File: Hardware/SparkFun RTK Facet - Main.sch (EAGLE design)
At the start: 99 parts, among them J1 QWIIC_RIGHT_ANGLE, J15 FPC_12_0.5MM2, J18 FPC_12_0.5MM2, J2 U.FL, J8 FPC_12_0.5MM2, Q2 MBT3904DW1T1, Q3 SIL2308, U1 74HC4052D, U10 MCP73833, U12 AP2112K-3.3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

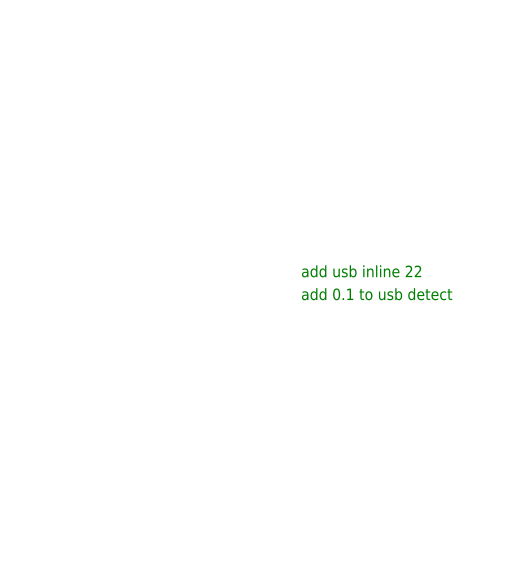
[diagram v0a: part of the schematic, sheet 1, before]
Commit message: Move display connector to side so overlay connector can be center. Notch PCBs. Add dummy PCB height. Add dummy retention plate.
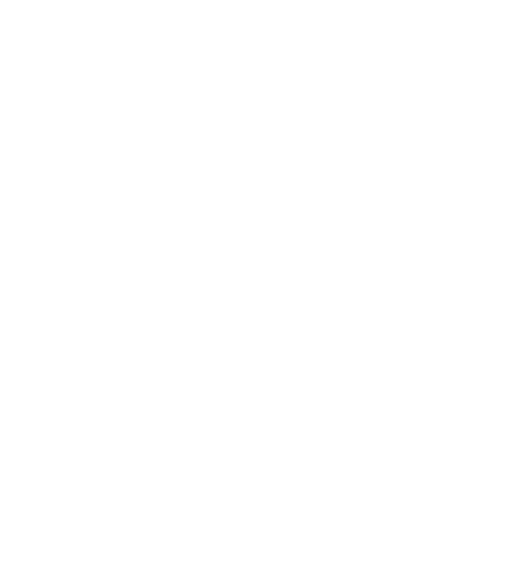
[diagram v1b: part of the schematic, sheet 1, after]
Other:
- note removed: "add 0.1 to usb detect"
- note removed: "add usb inline 22"
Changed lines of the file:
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@@
 <text x="332.74" y="132.08" size="1.27" layer="97" align="center">600mA Max
 55uA Quiescent</text>
-<text x="482.6" y="157.48" size="1.27" layer="91">add usb inline 22</text>
-<text x="482.6" y="154.94" size="1.27" layer="91">add 0.1 to usb detect</text>
 </plain>
 <instances>

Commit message: Update PROD ID on 12 pin connector. Add gerbers for v10.
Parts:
- J15, J18, J8: value FPC_12_0.5MM2 -> FPC_12_0.5MM_BACKFLIP; device RTK Facet:FPC_12_0.5MM2 -> RTK Facet:FPC_12_0.5MM_BACKFLIP
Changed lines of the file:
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@@
 <part name="SUPPLY7" library="SparkFun-PowerSymbols" deviceset="V_BATT" device=""/>
 <part name="GND20" library="SparkFun-PowerSymbols" deviceset="GND" device=""/>
-<part name="J15" library="RTK Facet" deviceset="FPC_12_0.5MM" device="2" value="FPC_12_0.5MM2"/>
+<part name="J15" library="RTK Facet" deviceset="FPC_12_0.5MM" device="_BACKFLIP" value="FPC_12_0.5MM_BACKFLIP"/>
 <part name="SUPPLY31" library="SparkFun-PowerSymbols" deviceset="3.3V" device=""/>
 <part name="GND28" library="SparkFun-PowerSymbols" deviceset="GND" device=""/>
-<part name="J18" library="RTK Facet" deviceset="FPC_12_0.5MM" device="2" value="FPC_12_0.5MM2"/>
+<part name="J18" library="RTK Facet" deviceset="FPC_12_0.5MM" device="_BACKFLIP" value="FPC_12_0.5MM_BACKFLIP"/>
 <part name="Q3" library="SparkFun-DiscreteSemi" deviceset="MOSFET_COMPLIMENTARY_PAIR" device="-SIL2308" value="SIL2308"/>
 <part name="C20" library="SparkFun-Capacitors" deviceset="22UF" device="-0603-6.3V-20%" value="22uF"/>
@@
 <part name="C29" library="SparkFun-Capacitors" deviceset="0.1UF" device="-0603-25V-5%" value="0.1uF"/>
 <part name="GND9" library="SparkFun-PowerSymbols" deviceset="GND" device=""/>
-<part name="J8" library="RTK Facet" deviceset="FPC_12_0.5MM" device="2" value="FPC_12_0.5MM2"/>
+<part name="J8" library="RTK Facet" deviceset="FPC_12_0.5MM" device="_BACKFLIP" value="FPC_12_0.5MM_BACKFLIP"/>
 </parts>
 <sheets>

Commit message: Move external connectors to button control. Add radio connector. Move ESP32 to VOUT. Move USB to VOUT. Remove USB from I2C.
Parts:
- removed J6: (no value), SparkFun-Connectors:CONN_041X04_NO_SILK_NO_POP
- added J10: FPC_12_0.5MM_BACKFLIP, RTK Facet:FPC_12_0.5MM_BACKFLIP
- added J3: (no value), SparkFun-Connectors:CONN_01PTH_NO_SILK_YES_STOP
- added J9: CORTEX_JTAG_DEBUG_PTH, SparkFun-Connectors:CORTEX_JTAG_DEBUG_PTH
- added JP1, JP2: JUMPER-SMT_2_NO_SILK, SparkFun-Jumpers:JUMPER-SMT_2_NO_SILK
- added R33, R34: 10k, SparkFun-Resistors:10KOHM-0603-1/10W-1%
- U4: value ADP160 -> STLQ015; device SparkFun-IC-Power:ADP160 -> SparkFun-IC-Power:STLQ015-3.3V
- U5: value ESP-WROOM-32NARROW -> ESP-WROOM-3232D-NARROW; device SparkFun-RF:ESP-WROOM-32NARROW -> SparkFun-RF:ESP-WROOM-3232D-NARROW
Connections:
- removed net ESP_0/BOOT: Q2Q2.C, U5.IO0
- removed net ESP_12/STAT_LED: R11.2, U5.MISO_H/IO12
- removed net ESP_13/POWER_CTRL: D4.A, R22.1, R24.2, U5.MOSI_H/IO13
- removed net ESP_14: J6.4, U5.SCK_H/IO14
- removed net ESP_15/FAST_OFF: C20.2, Q3G1.G, R24.1, U5.CS0_H/IO15
- removed net ESP_2/PERIPHERAL_POWER: R1.2, U12.EN, U5.IO2
- removed net ESP_27/ZED_!RESET!: R2D.2, U5.IO27
- removed net ESP_32: J6.3, U5.XTAL_P/IO32
- removed net ESP_33: J6.2, U5.XTAL_N/IO33
- removed net ESP_36/BATT_ALRT: U5.SENSOR_VP/I36, U7.!ALRT
- removed net ESP_4/MUX_A: U1.A, U5.IO4
- removed net ESP_5/MUX_B: U1.B, U5.CS0_V/IO5
- removed net ESP_I34/ZED_TX_READY: R9A.2, U5.I34
- removed net ESP_I35: J6.1, U5.I35
- new net ESP_0/BOOT/STAT_LED/MUX_B: Q2Q2.C, R11.2, U1.B, U5.IOA0
- new net ESP_12/MTDI/RADIO_NI: J10.4, J9.NC/TDI, U5.MISO2/IOA12
- new net ESP_13/POWER_CTRL/MTCK: D4.A, J9.SWDCLK/TCK, R22.1, R24.2, U5.MOSI2/IOA13
- new net ESP_14/PERIPHERAL_POWER/MTMS: J9.SWDIO/TMS, R1.2, U12.EN, U5.SCK2/IOA14
- new net ESP_15/MTDO/RADIO_!RESET!: J10.5, J9.SWO/TDO, U5.CS2/IOA15
- new net ESP_2/MUX_A: U1.A, U5.IOA2
- new net ESP_27/FAST_OFF: C20.2, Q3G1.G, R24.1, U5.IOA27
- new net ESP_32/RADIO_TXO: J10.11, U5.XTAL_P/IOA32
- new net ESP_33/RADIO_RXI: J10.10, U5.XTAL_N/IOA33
- new net ESP_4/RADIO_PWR_ON: J10.6, U5.IOA4
- new net ESP_5/RADIO_CTSI: J10.8, U5.CS3/IO5
- new net ESP_I34/RADIO_INT: J10.7, U5.IA34
- new net ESP_I35/DEVICE_SENSE: R33.2, R34.1, U5.IA35
- new net ESP_I36/RADIO_RTSO: J10.9, U5.SENSOR_VP/IA36
- new net N$21: JP1.2, U8.SDA
- new net N$23: JP2.2, U8.SCL/CFG0
- new net ZED_!RESET!: R2D.2
- new net ZED_TX_READY: R9A.2
- net 3.3V: now also J10.3; no longer C13.1, C14.1, R18.2, U6.V3, U6.VCC, U8.VDD33, U8.VDDA33
- net ESP32_EN: now also J9.!RESET
- net ESP32_RXI: now also U5.RX-IO3; no longer U5.RXD
- net ESP32_TXO: now also U5.TX-IO1; no longer U5.TXD
- net ESP_18/SD_SCK: now also U5.SCK3/IO18; no longer U5.SCK_V/IO18
- net ESP_19/SD_CIPO: now also U5.MISO3/IO19; no longer U5.MISO_V/IO19
- net ESP_21/SDA: now also JP1.1, U5.SDA/IO21; no longer U5.IO21, U8.SDA
- net ESP_22/SCL: now also JP2.1, U5.SCL/IO22; no longer U5.IO22, U8.SCL
- net ESP_23/SD_COPI: now also U5.MOSI3/IO23; no longer U5.MOSI_V/IO23
- net ESP_25/SD_!CS!: now also U5.DAC1/IOA25; no longer U5.IO25
- net ESP_26/DAC2: now also U5.DAC2/IOA26; no longer U5.IO26
- net ESP_3V3: now also C13.1, C14.1, J9.VCC, R18.2, R34.2, U6.V3, U6.VCC, U8.VDD33, U8.VDDA33
- net ESP_I39/ADC39: now also U5.SENSOR_VN/IA39; no longer U5.SENSOR_VN/I39
- net GND: now also J10.1, J10.2, J3.1, J9.GND@3, J9.GND@5, J9.GNDDTCT, J9.KEY, R33.1
- net N$14: now also U8.HS_IND/CFG1; no longer U8.HS_IND
- net VOUT: now also J10.12, J15.6, J15.7, J15.8, J15.9
- net V_BATT: no longer J15.6, J15.7, J15.8, J15.9
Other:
- note added: "1.5uA Quiescent"
- note added: "ADC2 has problems when WiFi is enabled."
- note added: "From Radio Board"
- note added: "IO0: Avoid device connections. Can be used a stat LED."
- note added: "IO12: Avoid external pullups - will cause bootloader fail."
- note added: "IO15: Has builtin pullup at POR."
- note added: "IO2: Avoid external pullups - will cause bootloader fail."
- note added: "IO5: Has builtin pullup at POR."
- note added: "Use boot control pins with caution: 0, 2, 5, 12, 15"
- note removed: "860nA Quiescent"
- note removed: "Can we indicate all on OLED: PPS RTK Stat Bluetooth Stat HPA Base Stat Batt Stat"
- moved on the sheet: D1, J7, MEAS2, R11
